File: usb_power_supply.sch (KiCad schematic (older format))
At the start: 9 parts, among them J4 USB_C_Receptacle_USB2.0, U4 AMS1117-3.3, U5 SRV05-4

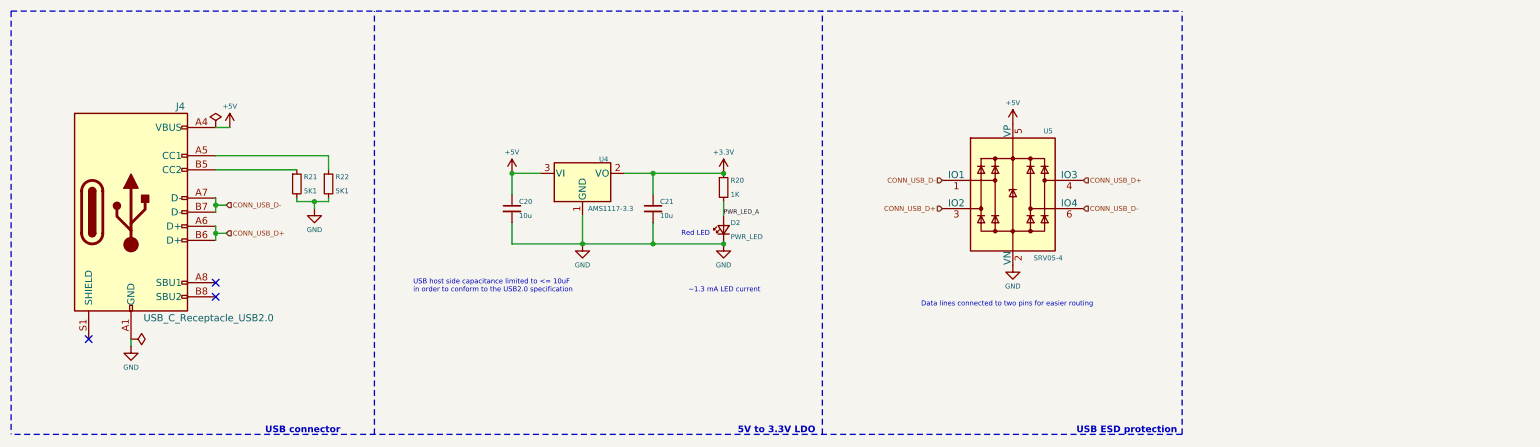
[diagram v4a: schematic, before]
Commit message: PCB: Rough component placement done
Signed-off-by: Tomislav Milkovic <tomislav.milkovic95@gmail.com>
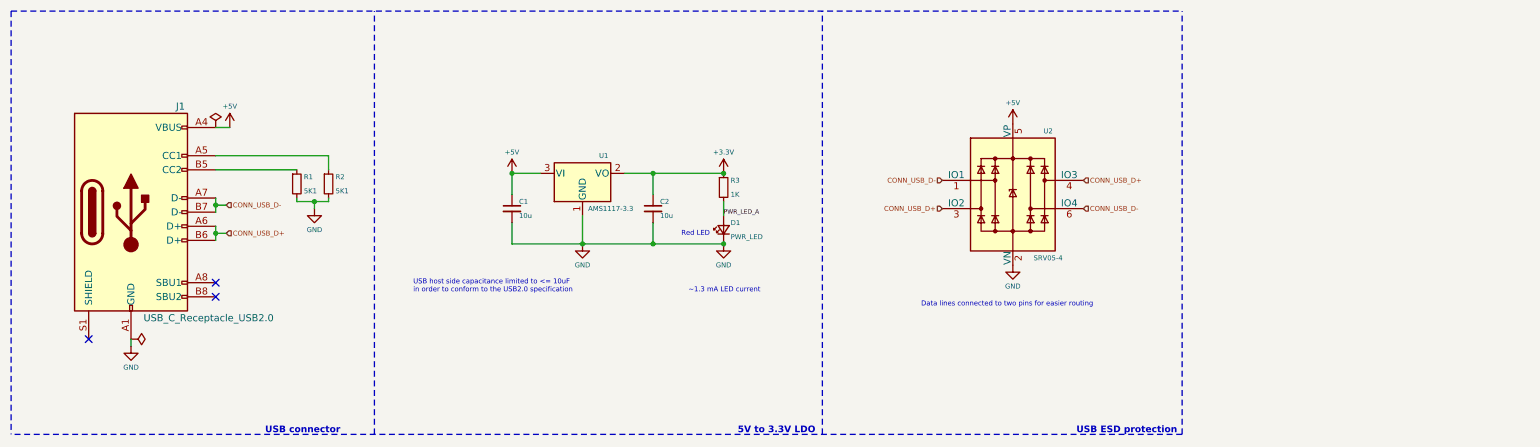
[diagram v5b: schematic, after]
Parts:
- renumbered C20 to C1, C21 to C2, D2 to D1, J4 to J1, R21 to R1, R22 to R2, R20 to R3, U4 to U1, U5 to U2
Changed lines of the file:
@@
 P 4550 1650
 AR Path="/63828FC7" Ref="U?"  Part="1"
-AR Path="/63818815/63828FC7" Ref="U4"  Part="1"
-F 0 "U4" H 4700 1750 35  0000 C CNN
+AR Path="/63818815/63828FC7" Ref="U1"  Part="1"
+F 0 "U1" H 4700 1775 35  0000 C CNN
 F 1 "AMS1117-3.3" H 4750 1400 35  0000 C CNN
 F 2 "Package_TO_SOT_SMD:SOT-223-3_TabPin2" H 4550 1850 50  0001 C CNN
@@
 P 4050 1900
 AR Path="/63828FD6" Ref="C?"  Part="1"
-AR Path="/63818815/63828FD6" Ref="C20"  Part="1"
-F 0 "C20" H 4100 1950 35  0000 L CNN
+AR Path="/63818815/63828FD6" Ref="C1"  Part="1"
+F 0 "C1" H 4100 1950 35  0000 L CNN
 F 1 "10u" H 4100 1850 35  0000 L CNN
 F 2 "Capacitor_SMD:C_0603_1608Metric" H 4050 1900 50  0001 C CNN
@@
 P 5050 1900
 AR Path="/63828FDD" Ref="C?"  Part="1"
-AR Path="/63818815/63828FDD" Ref="C21"  Part="1"
-F 0 "C21" H 5100 1950 35  0000 L CNN
+AR Path="/63818815/63828FDD" Ref="C2"  Part="1"
+F 0 "C2" H 5100 1950 35  0000 L CNN
 F 1 "10u" H 5100 1850 35  0000 L CNN
 F 2 "Capacitor_SMD:C_0603_1608Metric" H 5050 1900 50  0001 C CNN
@@
 P 5550 2050
 AR Path="/63828FE4" Ref="D?"  Part="1"
-AR Path="/63818815/63828FE4" Ref="D2"  Part="1"
-F 0 "D2" V 5600 2000 35  0000 R CNN
+AR Path="/63818815/63828FE4" Ref="D1"  Part="1"
+F 0 "D1" V 5600 2000 35  0000 R CNN
 F 1 "PWR_LED" V 5500 2000 35  0000 R CNN
 F 2 "LED_SMD:LED_0603_1608Metric" V 5550 2050 50  0001 C CNN
@@
 P 5550 1750
 AR Path="/63828FEB" Ref="R?"  Part="1"
-AR Path="/63818815/63828FEB" Ref="R20"  Part="1"
-F 0 "R20" H 5600 1800 35  0000 L CNN
+AR Path="/63818815/63828FEB" Ref="R3"  Part="1"
+F 0 "R3" H 5600 1800 35  0000 L CNN
 F 1 "1K" H 5600 1700 35  0000 L CNN
 F 2 "Resistor_SMD:R_0402_1005Metric" H 5550 1750 50  0001 C CNN
@@
 P 7600 1800
 AR Path="/6382903C" Ref="U?"  Part="1"
-AR Path="/63818815/6382903C" Ref="U5"  Part="1"
-F 0 "U5" H 7850 2250 35  0000 C CNN
+AR Path="/63818815/6382903C" Ref="U2"  Part="1"
+F 0 "U2" H 7850 2250 35  0000 C CNN
 F 1 "SRV05-4" H 7850 1350 35  0000 C CNN
 F 2 "Package_TO_SOT_SMD:SOT-23-6" H 8300 1350 50  0001 C CNN
@@
 	8800 3500 500  3500
 $Comp
-L Connector:USB_C_Receptacle_USB2.0 J4
+L Connector:USB_C_Receptacle_USB2.0 J1
 U 1 1 67B105B1
 P 1350 1925
-F 0 "J4" H 1700 2675 50  0000 C CNN
+F 0 "J1" H 1700 2675 50  0000 C CNN
 F 1 "USB_C_Receptacle_USB2.0" H 1900 1175 50  0000 C CNN
 F 2 "Connector_USB:USB_C_Receptacle_XKB_U262-16XN-4BVC11" H 1500 1925 50  0001 C CNN
@@
 P 2750 1725
 AR Path="/67B3BFCC" Ref="R?"  Part="1"
-AR Path="/63818815/67B3BFCC" Ref="R22"  Part="1"
-F 0 "R22" H 2800 1775 35  0000 L CNN
+AR Path="/63818815/67B3BFCC" Ref="R2"  Part="1"
+F 0 "R2" H 2800 1775 35  0000 L CNN
 F 1 "5K1" H 2800 1675 35  0000 L CNN
 F 2 "Resistor_SMD:R_0402_1005Metric" H 2750 1725 50  0001 C CNN
@@
 P 2525 1725
 AR Path="/67B3A44D" Ref="R?"  Part="1"
-AR Path="/63818815/67B3A44D" Ref="R21"  Part="1"
-F 0 "R21" H 2575 1775 35  0000 L CNN
+AR Path="/63818815/67B3A44D" Ref="R1"  Part="1"
+F 0 "R1" H 2575 1775 35  0000 L CNN
 F 1 "5K1" H 2575 1675 35  0000 L CNN
 F 2 "Resistor_SMD:R_0402_1005Metric" H 2525 1725 50  0001 C CNN

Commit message: Add fiducials, finish routing
Signed-off-by: Tomislav Milkovic <tomislav.milkovic95@gmail.com>
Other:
- note added: "Data lines connected to two pins for easier routing\n(additional capacity is insignificant for USB2.0 HS speeds)"
- note removed: "Data lines connected to two pins for easier routing"
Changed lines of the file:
@@
 Text Notes 5300 2500 0    35   ~ 0
 ~~1.3 mA LED current
-Text Notes 6950 2600 0    35   ~ 0
-Data lines connected to two pins for easier routing
+Text Notes 6950 2750 0    35   ~ 0
+Data lines connected to two pins for easier routing\n(additional capacity is insignificant for USB2.0 HS speeds)
 Text HLabel 8100 1700 2    35   Input ~ 0
 CONN_USB_D+
